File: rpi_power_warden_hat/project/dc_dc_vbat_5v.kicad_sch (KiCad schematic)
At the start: 14 parts, among them Q2 FDS4435BZ, U3 LM3489MM

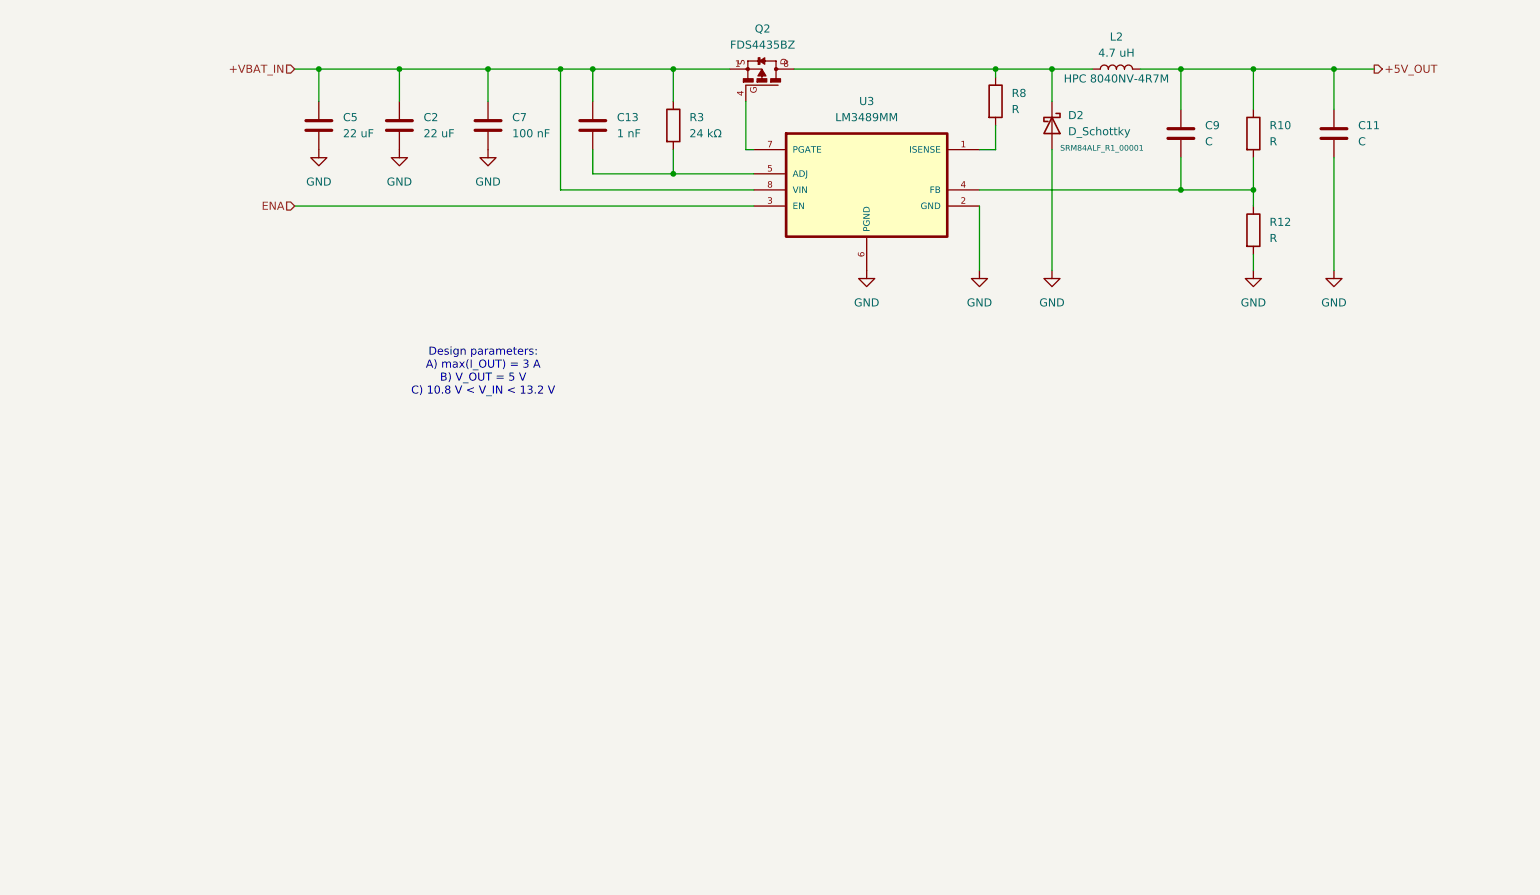
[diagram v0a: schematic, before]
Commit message: feat: put USB A receptacle to deliver power, have progress in INA260 and place test poitns
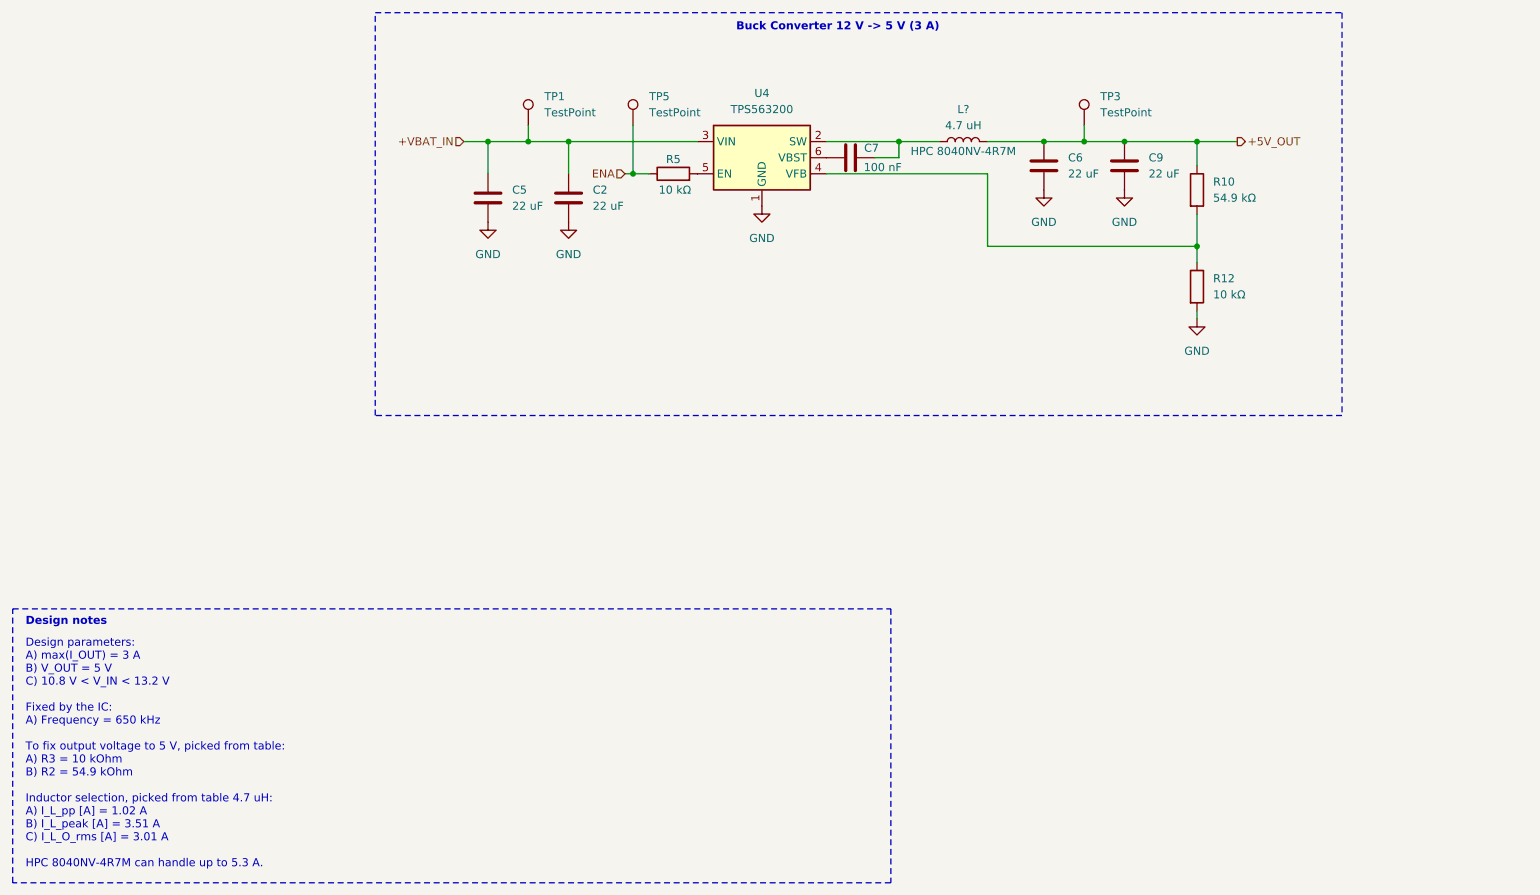
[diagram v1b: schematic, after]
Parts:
- removed C11: C, symbol Device:C
- removed C13: 1 nF, Capacitor_SMD:C_0603_1608Metric_Pad1.08x0.95mm_HandSolder, symbol Device:C
- removed D2: D_Schottky, rpi_power_warden_hat:D_DO-221AA, symbol Device:D_Schottky
- removed Q2: FDS4435BZ, FDS4435BZ:SO08-E3, symbol rpi_power_warden_hat:FDS4435BZ
- removed R3: 24 kΩ, Resistor_SMD:R_0603_1608Metric_Pad0.98x0.95mm_HandSolder, symbol Device:R
- removed R8: R, symbol Device:R
- removed U3: LM3489MM, rpi_power_warden_hat:SOP65P490X110-8N, symbol rpi_power_warden_hat:LM3489MM
- added C6: 22 uF, Capacitor_SMD:C_0805_2012Metric_Pad1.18x1.45mm_HandSolder, symbol Device:C
- added R5: 10 kΩ, Resistor_SMD:R_0603_1608Metric_Pad0.98x0.95mm_HandSolder, symbol Device:R
- added TP1, TP3, TP5: TestPoint, TestPoint:TestPoint_Pad_D2.5mm, symbol Connector:TestPoint
- added U4: TPS563200, rpi_power_warden_hat:SOT-23-6, symbol rpi_power_warden_hat:TPS563200
- C9: value C -> 22 uF; footprint (none) -> Capacitor_SMD:C_0805_2012Metric_Pad1.18x1.45mm_HandSolder; manufacturer (none) -> Murata Electronics; mpn (none) -> GRM21BR61E226ME44L
- R10: value R -> 54.9 kΩ; footprint (none) -> Resistor_SMD:R_0603_1608Metric_Pad0.98x0.95mm_HandSolder; manufacturer (none) -> Panasonic Electronic Components; mpn (none) -> ERJ-3EKF5492V
- R12: value R -> 10 kΩ; footprint (none) -> Resistor_SMD:R_0603_1608Metric_Pad0.98x0.95mm_HandSolder; manufacturer (none) -> Panasonic Electronic Components; mpn (none) -> ERJ-3EKF1002V
- renumbered L2 to L?
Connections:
- net +5V_OUT: now also C6.1, TP3.1
- net +VBAT_IN: now also TP1.1, U4.3 (VIN); no longer C7.1
- net ENA: now also R5.1, TP5.1
- net GND: now also C9.2, C6.2, U4.1 (GND); no longer C7.2
- net at L?.1: now also C7.2, U4.2 (SW)
- net at R10.2, R12.1: now also U4.4 (VFB); no longer C9.2
- new net: C7.1, U4.6 (VBST)
- new net: R5.2, U4.5 (EN)
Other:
- note added: "Buck Converter 12 V -> 5 V (3 A)"
- note added: "Design notes"
- note added: "Design parameters: A) max(I_OUT) = 3 A B) V_OUT = 5 V C) 10.8 V < V_IN < 13.2 V Fixed by the IC: A) Frequency = 650 kHz To fix output voltage to 5 V, picked from table: A) R3 = 10 kOhm B) R2 = 54.9 kOhm Inductor selection, picked from table 4.7 uH: A) I_L_pp [A] = 1.02 A B) I_L_peak [A] = 3.51 A C) I_L_O_rms [A] = 3.01 A HPC 8040NV-4R7M can handle up to 5.3 A."
- note removed: "Design parameters: A) max(I_OUT) = 3 A B) V_OUT = 5 V C) 10.8 V < V_IN < 13.2 V"
- moved on the sheet: C2, C5, L?, R10, R12

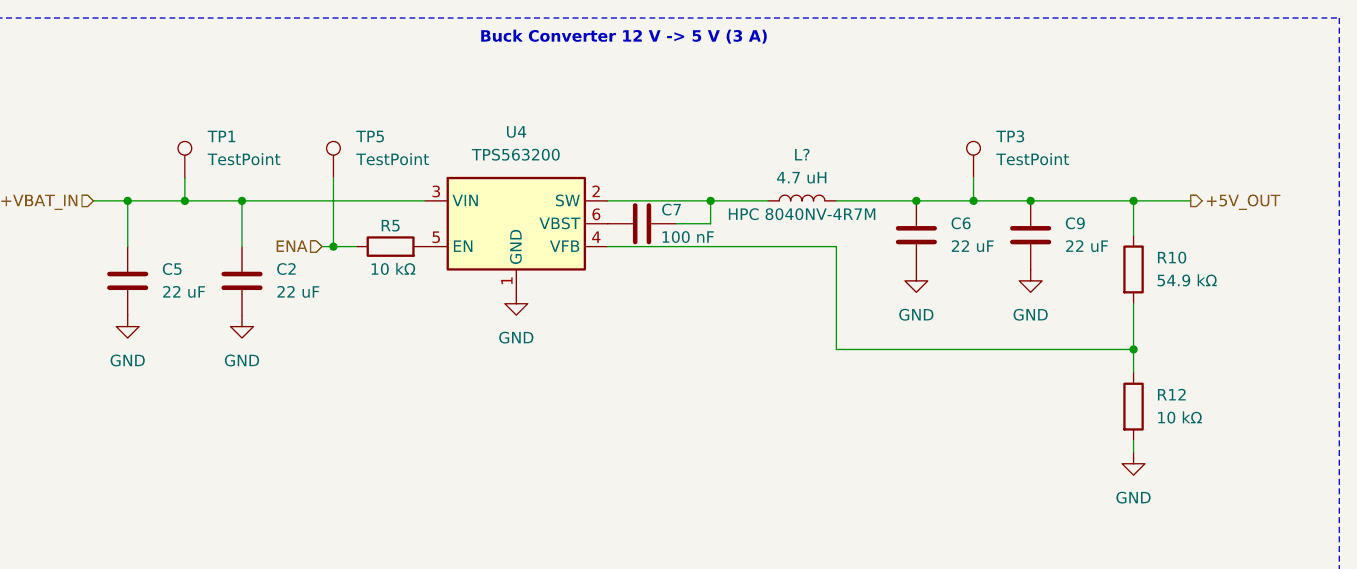
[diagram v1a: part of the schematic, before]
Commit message: add a switched vbat feature
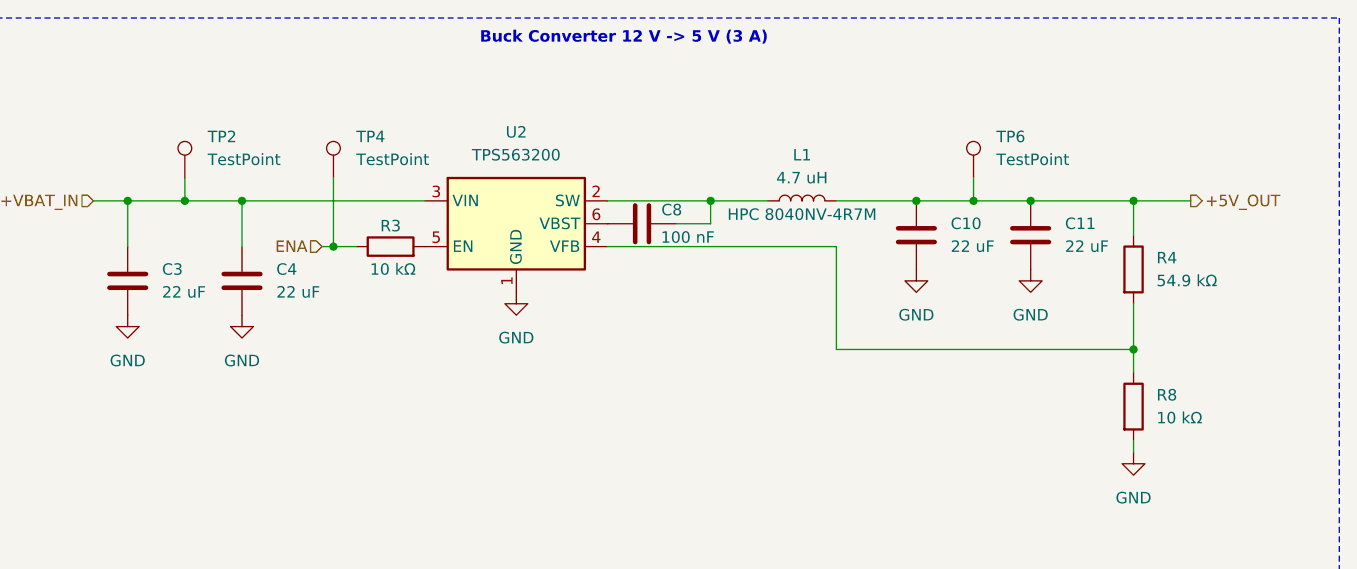
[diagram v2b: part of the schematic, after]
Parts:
- gave numbers to parts that had none: 1
- renumbered C6 to C10, C9 to C11, C5 to C3, C2 to C4, C7 to C8, R5 to R3, R10 to R4, R12 to R8, TP1 to TP2, TP5 to TP4, TP3 to TP6, U4 to U2

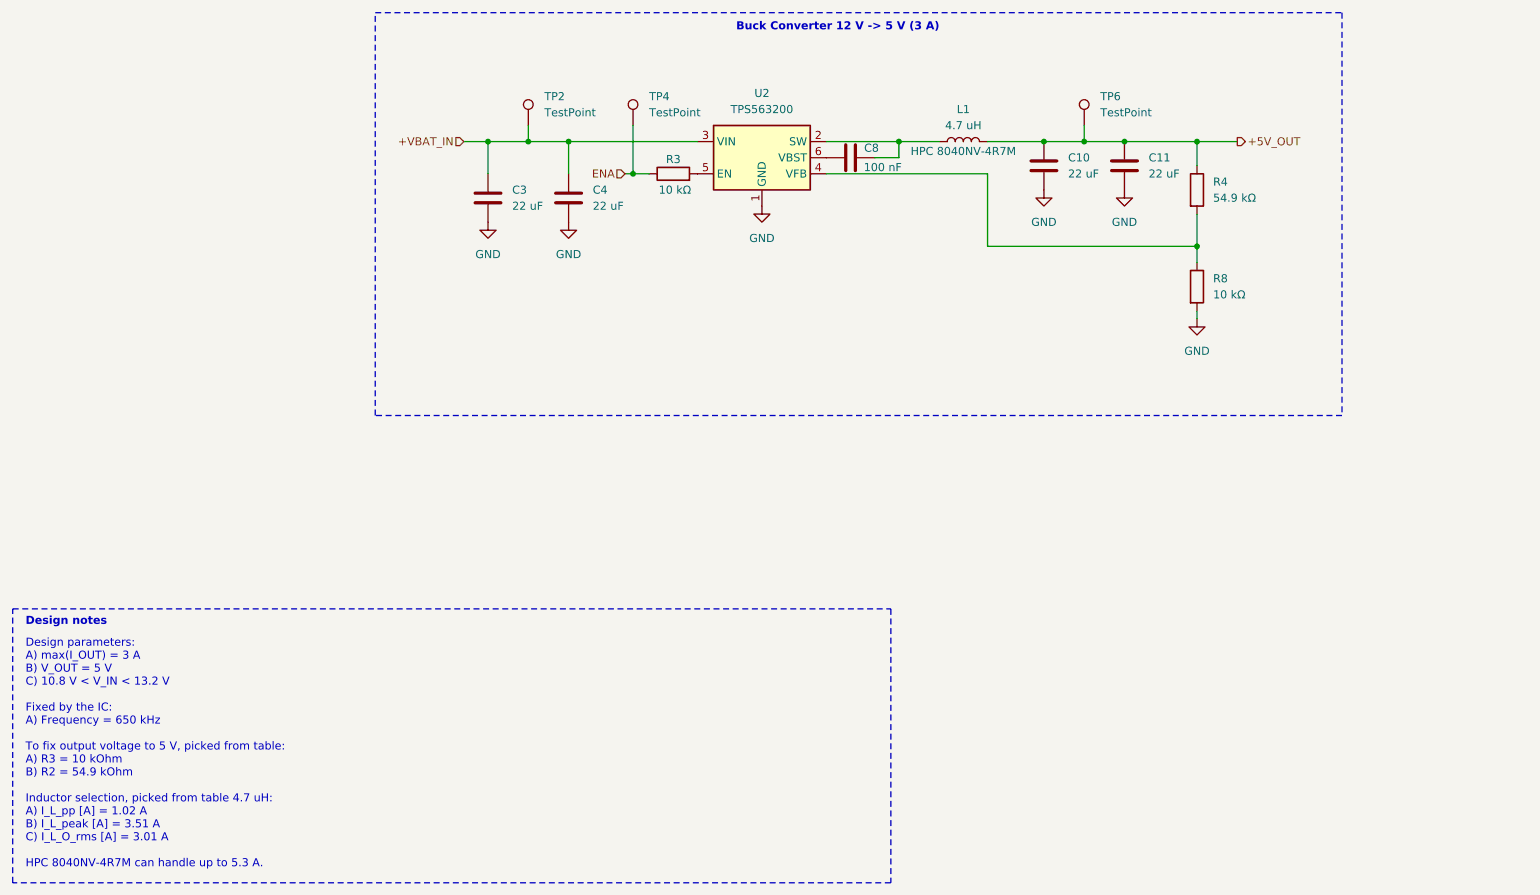
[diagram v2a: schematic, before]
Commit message: re-annotate schematic, add leds to power supply outputs and add connector for VBAT switched load
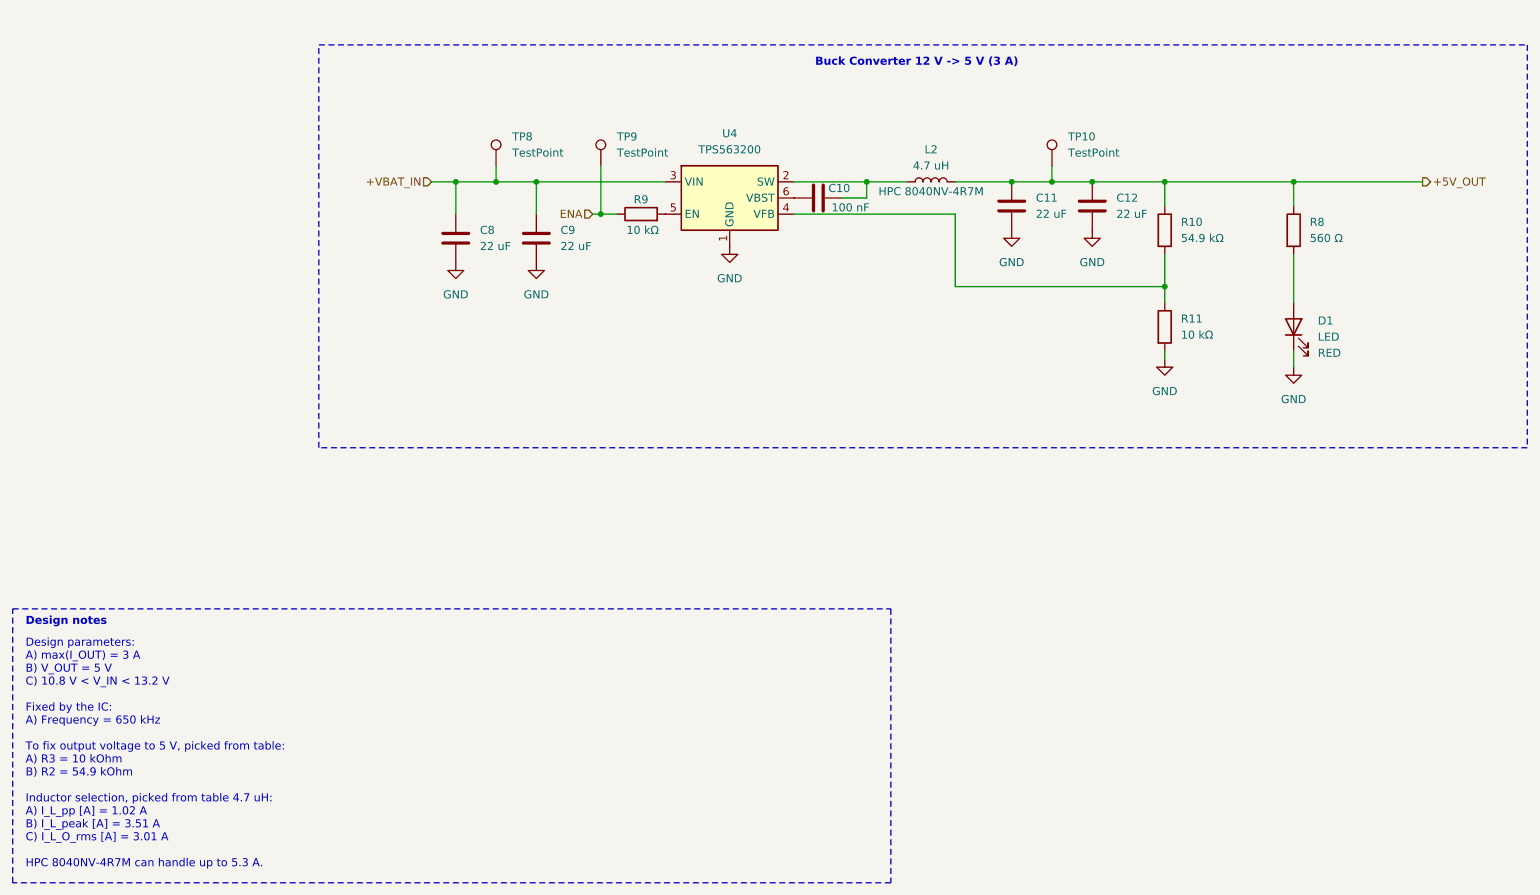
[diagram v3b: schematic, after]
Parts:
- added D1: LED, LED_SMD:LED_0603_1608Metric, symbol Device:LED
- added R8: 560 Ω, Resistor_SMD:R_0603_1608Metric_Pad0.98x0.95mm_HandSolder, symbol Device:R
- renumbered C8 to C10, C10 to C11, C11 to C12, C3 to C8, C4 to C9, L1 to L2, R4 to R10, R8 to R11, R3 to R9, TP6 to TP10, TP2 to TP8, TP4 to TP9, U2 to U4
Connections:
- net +5V_OUT: now also R8.1
- net GND: now also D1.1 (K)
- new net: D1.2 (A), R8.2
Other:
- moved on the sheet: C10, C11, C12, C8, C9, L2, R10, R11, R9, TP10, TP8, TP9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
